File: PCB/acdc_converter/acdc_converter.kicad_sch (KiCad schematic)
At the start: 0 parts

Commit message: Add two-bucket isolated PSU and the PC analysis software
PSU (PCB/acdc_converter/design.py, generated schematic, ERC clean):
Mains -> IRM-05-15 -> LM317 constant-current (0.2 A) / constant-voltage
(10.9 V) supercap charger -> two 4 x 10 F buckets swapped every ~30 s by
two Omron G6K-2 DPDT relays wired in opposite senses. Form-C contacts
break before make, so the receiver ground is never connected to the
charger side; the only coupling left is the open-contact capacitance
(~1 pF) instead of the AC-DC barrier (20-100 pF). The receiver side
adds a reservoir, an LT3045 (0.8 uV rms, EN/PGFB to IN, 22 uF C_SET for
low 1/f noise) and a common-mode choke. Charger ground is bonded to PE
and the enclosure; the only LED is on the mains-powered charger side.

Software (software/elara): streaming decimator, PLL-locked NLMS mains
canceller (>60 dB with drift, 45 Hz tone untouched), L/R Wiener noise
reference subtraction, front-end response correction, Lorentzian
Schumann fit, sferic detector, simulator and CLI; 27 pytest tests.

Generator: explicit wires, net labels on wires, touching and stacked
pins, labels-only symbols.

Co-Authored-By: Claude Opus 5.5 <noreply@anthropic.com>
Claude-Session: https://claude.ai/code/session_01RsM1DhHhY1tSr2aHjVygSC
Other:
- added sheet Two-bucket isolated supply (psu.kicad_sch)
- company: (none) -> ELARA -- ELF Atmospheric Radio Analyser
- title: (none) -> ELARA PSU
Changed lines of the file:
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@@
 	(generator_version "9.0")
 	(paper "A4")
+	(title_block
+		(title "ELARA PSU")
+		(rev "0.2")
+		(company "ELARA -- ELF Atmospheric Radio Analyser")
+		(comment 1 "CERN-OHL-W-2.0")
+		(comment 2 "Generated by PCB/acdc_converter/design.py -- edit the script, not the sheet")
+		(comment 3 "MAINS VOLTAGE on the primary side -- 6.4 mm creepage to everything else")
+	)
+	(sheet
+		(at 25.4 38.1)
+		(size 63.5 25.4)
+		(exclude_from_sim no)
+		(in_bom yes)
+		(on_board yes)
+		(dnp no)
+		(fields_autoplaced yes)
+		(stroke
+			(width 0.1524)
+			(type solid)
+		)
+		(fill
+			(color 0 0 0 0)
+		)
+		(property "Sheetname" "Two-bucket isolated supply"
+			(at 25.4 37.4 0)
+			(effects
+				(font
+					(size 1.27 1.27)
+				)
+				(justify left bottom)
+			)
+		)
+		(property "Sheetfile" "psu.kicad_sch"
+			(at 25.4 64.1 0)
+			(effects
+				(font
+					(size 1.27 1.27)
+				)
+				(justify left top)
+			)
+		)
+		(instances
+			(project "acdc_converter"
+				(path "/51f97529-9367-5829-99b3-c24681f1e347"
+					(page "2")
+				)
+			)
+		)
+	)
 	(sheet_instances
 		(path "/"

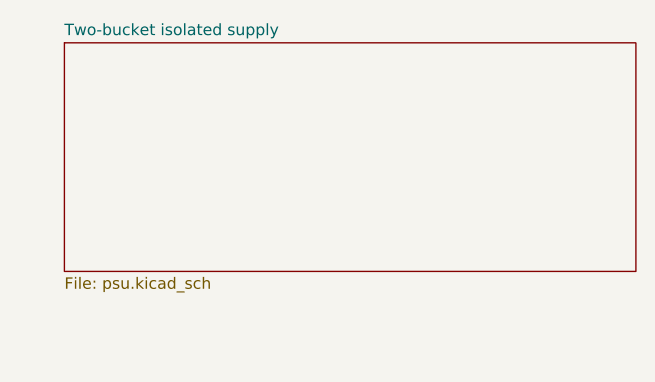
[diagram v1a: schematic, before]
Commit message: Pedantic schematic and silkscreen pass: zero overlaps, labels clear of tracks
Schematics
- tools/kicadgen/schcheck.py checks KiCad's own SVG rendering (exact stroke boxes)
  for text over text, lines through text, crowded twin labels and text outside the
  frame. Both schematics: 0 findings; ERC 0 on both.
- Generator: Sheet.join (one wire + one label instead of two facing labels),
  per-symbol field positions, per-pin stub lengths, shared power symbol for
  adjacent top/bottom rail pins, crowded rail runs get one label, longer PCM1804
  pins (no-connect cross clear of the pin number), PE value clear of its symbol.
- Fixed: doubled VIN_RAW/BIAS_DIV/LED_OVF/CV_ADJ/LED_C labels, +5VA vs VREG,
  +5V_PRE twins, CS8406 GND straps vs neighbours, BNC/LED/diode fields over their
  graphics, bucket-cell values vs tap labels, notes outside the frame, J2 -> J202.
- Root sheet: sub-sheets in signal-flow order with arrows and a design summary;
  dated title blocks.

Boards
- References prefer spots clear of tracks as well as parts (two candidate rings);
  compartment labels are re-placed after routing; the title block on the back is
  placed as one unit; no stitching via under any board text.
- DRC with schematic parity: amplifier 0 errors / 0 unconnected / 0 parity (only
  the intended bare-island mask warnings); PSU and plate 0 of anything.

Co-Authored-By: Claude Opus 5.5 <noreply@anthropic.com>
Claude-Session: https://claude.ai/code/session_01RsM1DhHhY1tSr2aHjVygSC
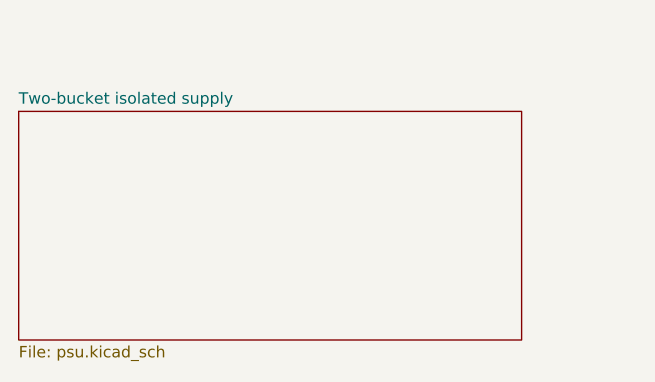
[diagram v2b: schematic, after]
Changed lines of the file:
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@@
 	(title_block
 		(title "ELARA PSU")
+		(date "2026-09-30")
 		(rev "0.2")
 		(company "ELARA -- ELF Atmospheric Radio Analyser")
@@
 	)
 	(sheet
-		(at 25.4 38.1)
-		(size 63.5 25.4)
+		(at 20.32 45.72)
+		(size 55.88 25.4)
 		(exclude_from_sim no)
 		(in_bom yes)
@@
 		)
 		(property "Sheetname" "Two-bucket isolated supply"
-			(at 25.4 37.4 0)
+			(at 20.32 45.02 0)
 			(effects
 				(font
@@
 		)
 		(property "Sheetfile" "psu.kicad_sch"
-			(at 25.4 64.1 0)
+			(at 20.32 71.72 0)
 			(effects
 				(font

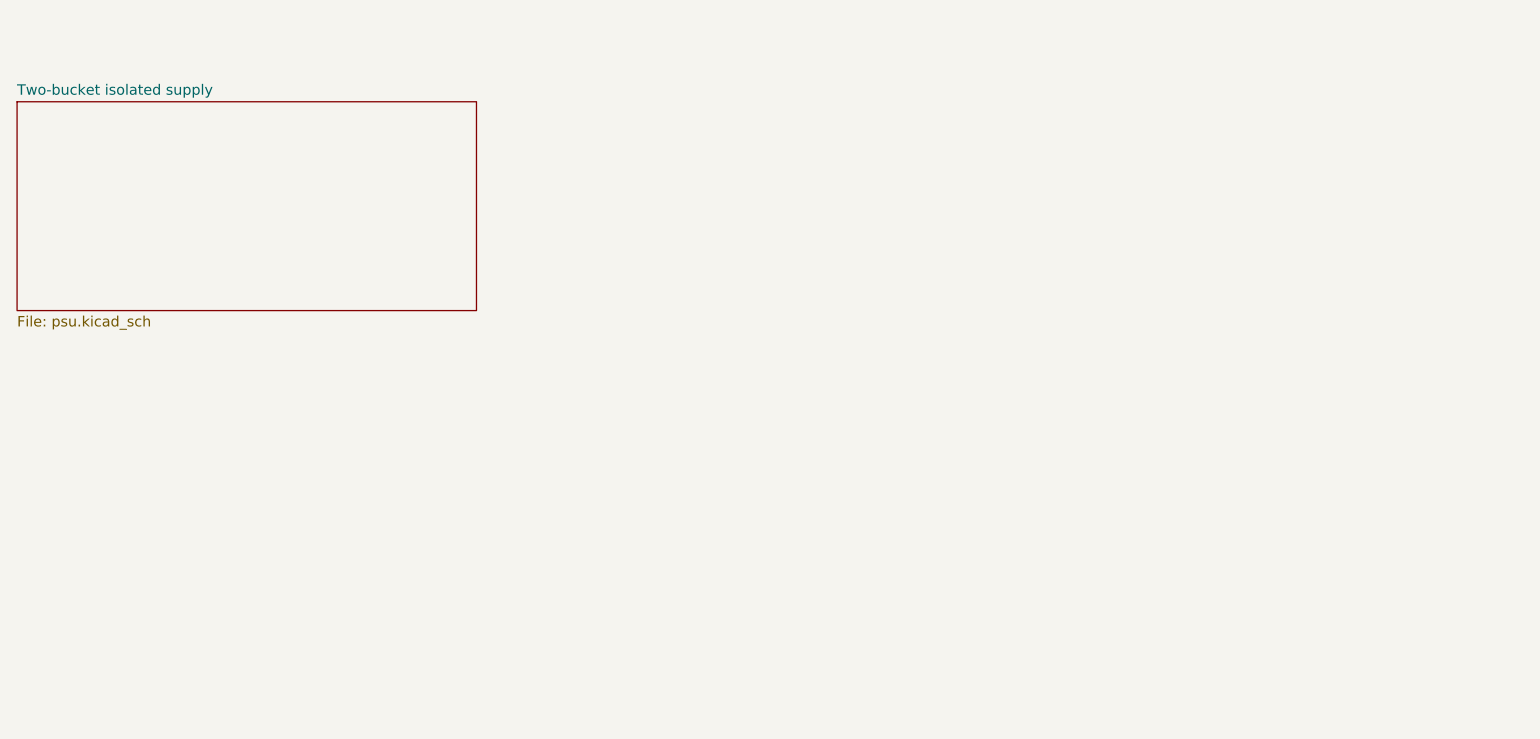
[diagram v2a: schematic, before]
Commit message: AES3 source resistors 22 ohm for a 111 ohm source; tidy schematics and assembly drawings
- R412/R413 2 x 39 -> 2 x 22 ohm (Vishay TNPW060322R0BEEA, anti-sulfur): the
  CS8406 drivers are 33.5 ohm each at VL = 3.3 V, so 2 x 39 gave a 145 ohm
  source, outside AES3's 110 ohm +-20 %. The schematic note had used the 5 V
  figure and mis-added it.
- AES3 sheet: transformer flipped (kicadgen gains mirror='x') and wired straight
  to R412/R413/C405 and the RJ45, no more touching AES_HOT/AES_COLD labels.
- Stale S/PDIF and 9 V wording out of the sheets and BOM: DC input block reads
  6.98-15 V, J101 'DC IN', PSU J2 'DC OUT', reset button and clock branch say
  AES3; the legacy +9V / +9V_OUT net names are explained on the sheets.
- PSU root sheet gets the same power-path / board summary as the amplifier.
- Assembly drawings: fab-layer copies of the references removed wherever the
  silk reference shows (KiCad 9 texts cannot be hidden), so each part is named
  once; J201/J202 (no silk on the guard island) get theirs beside the part.
- BOM totals +0.14 EUR (502.15 ex VAT reference build, 407.22 recommended).

Co-Authored-By: Claude Opus 5.5 <noreply@anthropic.com>
Claude-Session: https://claude.ai/code/session_01RsM1DhHhY1tSr2aHjVygSC
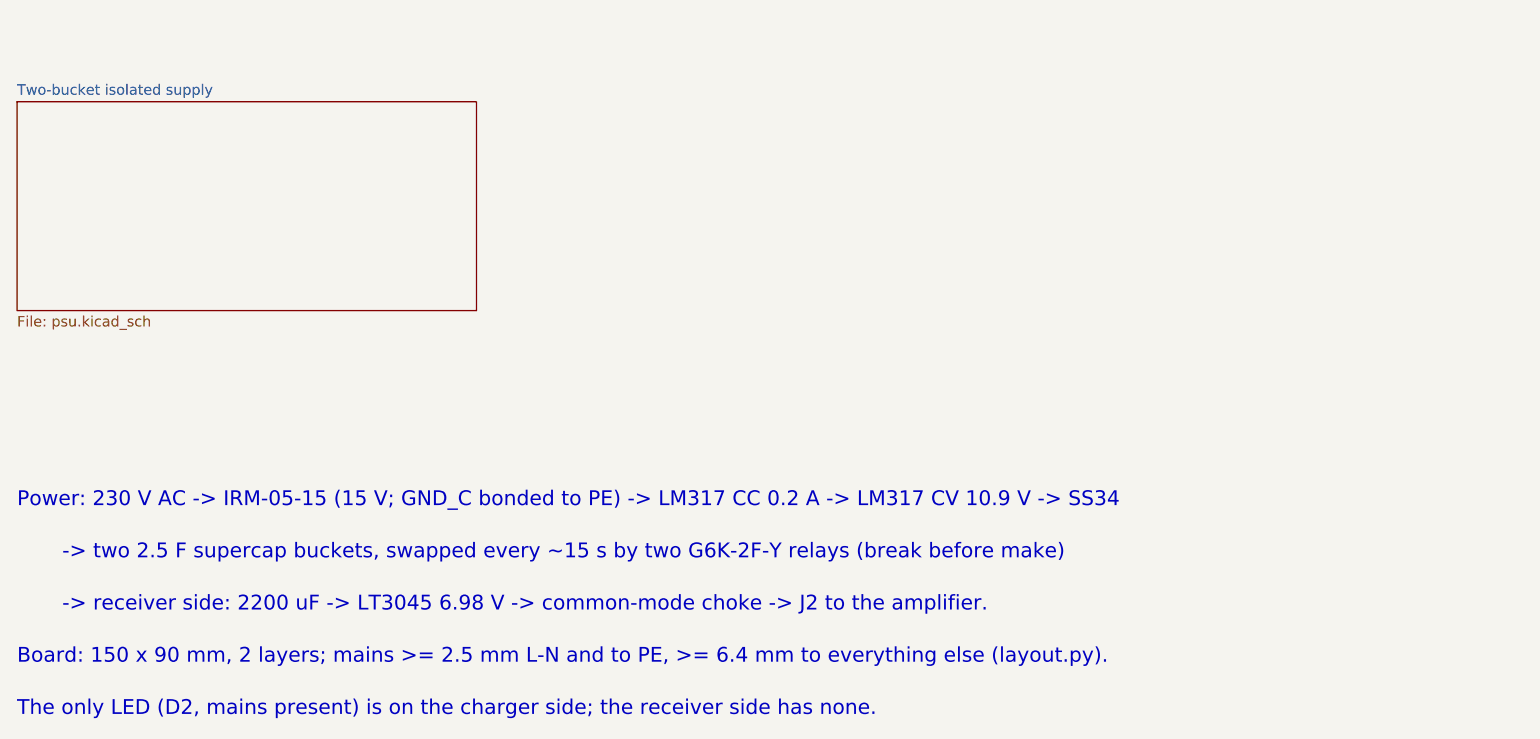
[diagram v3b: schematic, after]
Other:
- note added: "-> receiver side: 2200 uF -> LT3045 6.98 V -> common-mode choke -> J2 to the amplifier."
- note added: "-> two 2.5 F supercap buckets, swapped every ~15 s by two G6K-2F-Y relays (break before make)"
- note added: "Board: 150 x 90 mm, 2 layers; mains >= 2.5 mm L-N and to PE, >= 6.4 mm to everything else (layout.py)."
- note added: "Power: 230 V AC -> IRM-05-15 (15 V; GND_C bonded to PE) -> LM317 CC 0.2 A -> LM317 CV 10.9 V -> SS34"
- note added: "The only LED (D2, mains present) is on the charger side; the receiver side has none."
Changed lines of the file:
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@@
+		)
+	)
+	(text "Power: 230 V AC -> IRM-05-15 (15 V; GND_C bonded to PE) -> LM317 CC 0.2 A -> LM317 CV 10.9 V -> SS34"
+		(exclude_from_sim no)
+		(at 20.32 95.25 0)
+		(effects
+			(font
+				(size 1.8 1.8)
+			)
+			(justify left bottom)
+		)
+	)
+	(text "       -> two 2.5 F supercap buckets, swapped every ~15 s by two G6K-2F-Y relays (break before make)"
+		(exclude_from_sim no)
+		(at 20.32 101.6 0)
+		(effects
+			(font
+				(size 1.8 1.8)
+			)
+			(justify left bottom)
+		)
+	)
+	(text "       -> receiver side: 2200 uF -> LT3045 6.98 V -> common-mode choke -> J2 to the amplifier."
+		(exclude_from_sim no)
+		(at 20.32 107.95 0)
+		(effects
+			(font
+				(size 1.8 1.8)
+			)
+			(justify left bottom)
+		)
+	)
+	(text "Board: 150 x 90 mm, 2 layers; mains >= 2.5 mm L-N and to PE, >= 6.4 mm to everything else (layout.py)."
+		(exclude_from_sim no)
+		(at 20.32 114.3 0)
+		(effects
+			(font
+				(size 1.8 1.8)
+			)
+			(justify left bottom)
+		)
+	)
+	(text "The only LED (D2, mains present) is on the charger side; the receiver side has none."
+		(exclude_from_sim no)
+		(at 20.32 120.65 0)
+		(effects
+			(font
+				(size 1.8 1.8)
+			)
+			(justify left bottom)
 		)
 	)

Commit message: PSU charger at 10.4 V so the 2.7 V cells stay in rating; charger model corrected
The LM317 CV divider (240 R / 1.87 k) set 11.08 V, not the 10.9 V it was
labelled with: 2.72 V per EDLC cell whenever the receiver draws nothing,
2.83 V at the LM317's limits. R4 is now 1.74 k (10.4 V, 2.55 V per cell,
2.70 V worst case). Board copper and placement are unchanged; only R4's
value, the BOM and the order lists change.

The PSU model's charger now drops 6.2 ohm x I in the CC stage below 0.2 A
instead of a fixed 1.25 V. Re-run: 1.81 V of LT3045 headroom nominal,
1.05 V with every corner stacked. A 30 s swap is added as an option case
(0.36 V stacked), which replaces STATUS's unbacked claim that it drops out.
Also: the amplifier's +9V bus is about 6.0 V from the PSU (not 6.6 V),
and the PSU README's circuit line, CMC loop and margin figures are fixed.

Co-Authored-By: Claude Opus 5.5 <noreply@anthropic.com>
Claude-Session: https://claude.ai/code/session_01RsM1DhHhY1tSr2aHjVygSC
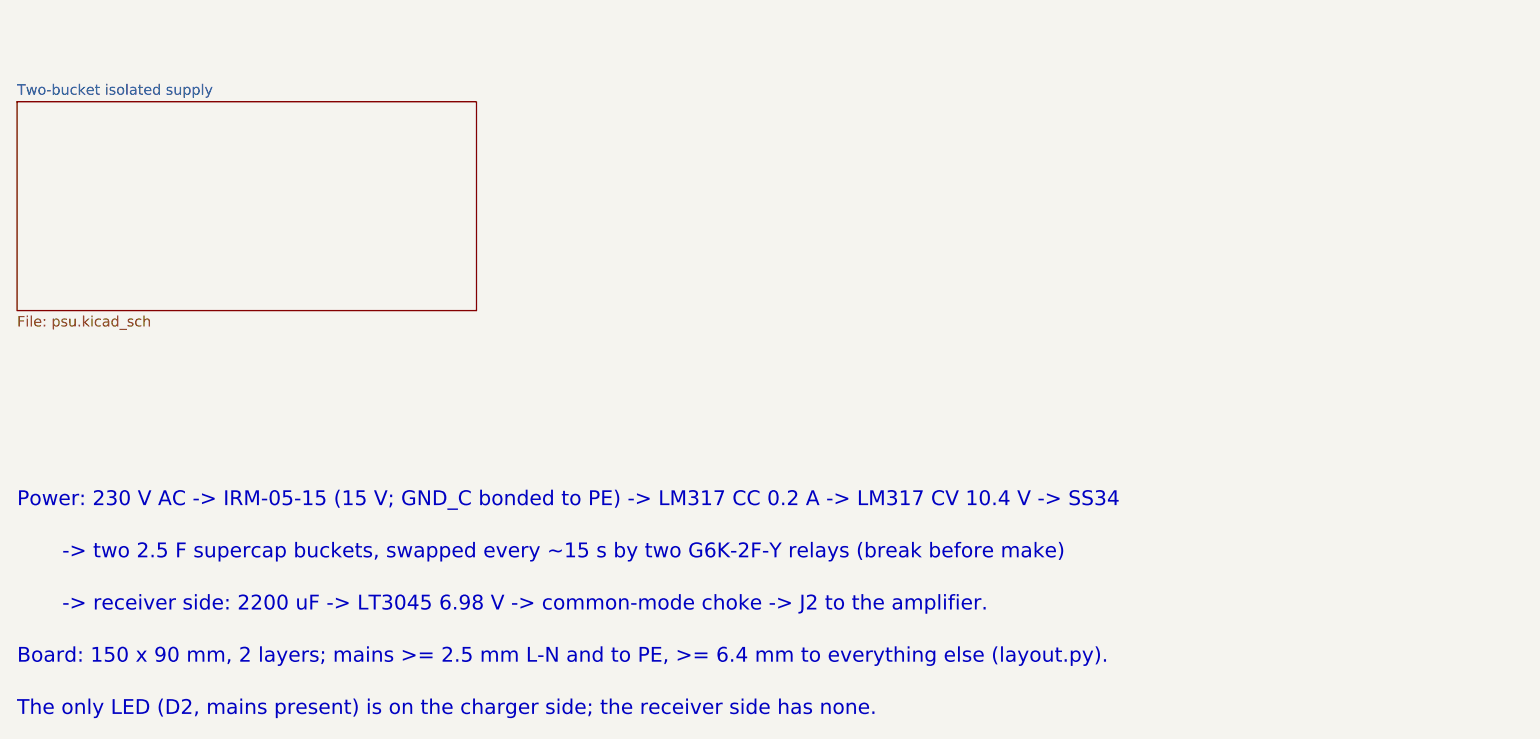
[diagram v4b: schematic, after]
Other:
- note added: "Power: 230 V AC -> IRM-05-15 (15 V; GND_C bonded to PE) -> LM317 CC 0.2 A -> LM317 CV 10.4 V -> SS34"
- note removed: "Power: 230 V AC -> IRM-05-15 (15 V; GND_C bonded to PE) -> LM317 CC 0.2 A -> LM317 CV 10.9 V -> SS34"
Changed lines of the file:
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@@
 		)
 	)
-	(text "Power: 230 V AC -> IRM-05-15 (15 V; GND_C bonded to PE) -> LM317 CC 0.2 A -> LM317 CV 10.9 V -> SS34"
+	(text "Power: 230 V AC -> IRM-05-15 (15 V; GND_C bonded to PE) -> LM317 CC 0.2 A -> LM317 CV 10.4 V -> SS34"
 		(exclude_from_sim no)
 		(at 20.32 95.25 0)
